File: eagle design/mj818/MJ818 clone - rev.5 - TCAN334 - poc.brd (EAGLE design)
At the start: 35 x 35 mm, 36 parts, among them IC202 LDK320AM33R, IC302 STM32F042G6U6, IC401 TCAN334, IC506 MAX16820, IC507 SQA470EEJ-T1_GE3, IC601 MAX16839, J101 Power Supply, J102 LED, J103 CAN

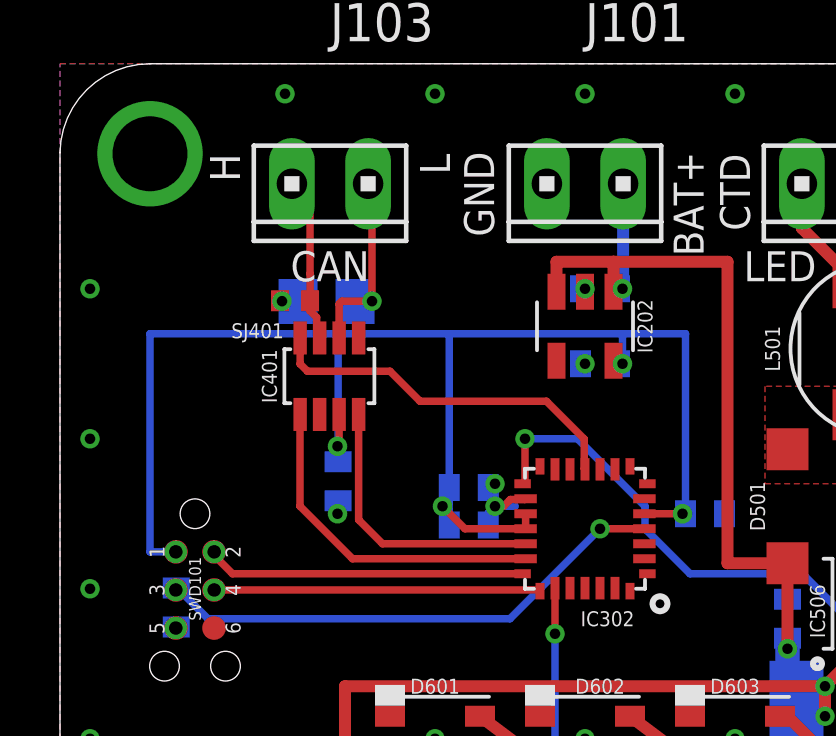
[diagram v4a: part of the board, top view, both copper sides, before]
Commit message: - added CAN split termination with two 60 Ohm resistors and one 47nF ceramic capacitor.
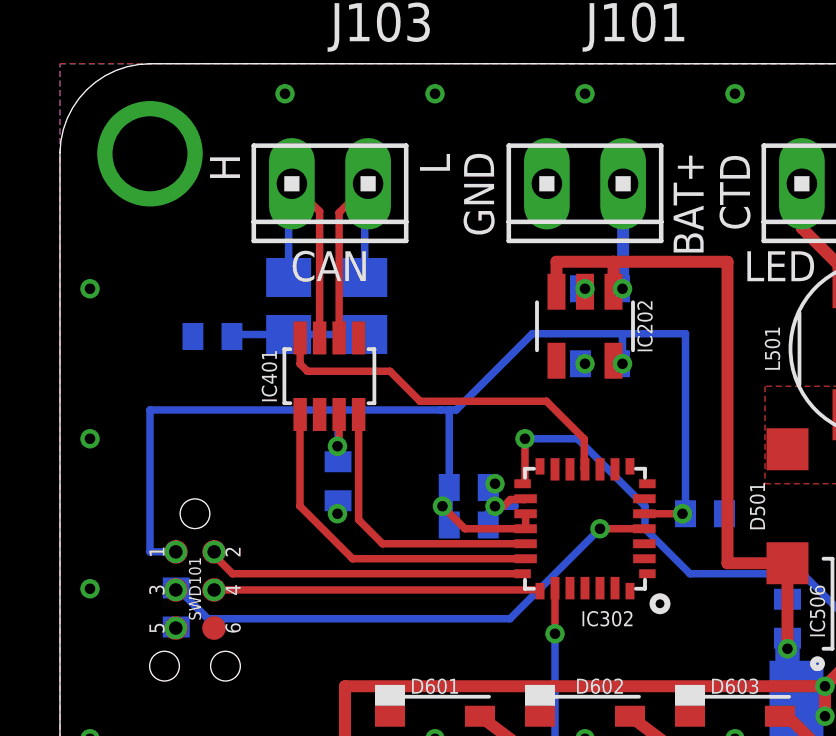
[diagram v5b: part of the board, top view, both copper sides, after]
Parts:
- removed SJ401: CAN termination, rcl:R0402
- added C401: 47nF, rcl:C0402
- added R401: 60, rcl:R0805
- R405: value 120 -> 60
- moved R405 1.28 mm to (10.2, 26.9), turned to 270 degrees
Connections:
- removed net CAN_INFRA:CAN_JMPR: R405.2, SJ401.1
- new net CAN_INFRA:SPLIT: C401.1, R401.1, R405.2
- net CAN_H: now also R401.2; no longer SJ401.2
- net GND: now also C401.2
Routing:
- net 3V3: track 51.1 -> 44.5 mm
- net CAN_INFRA:SPLIT: track 0.00 -> 4.46 mm
- net CAN_H: track 5.52 -> 8.69 mm
- net CAN_L: track 6.81 -> 8.71 mm, vias 1 -> 0
- net CAN_INFRA:CAN_JMPR: track 0.63 -> 0.00 mm, vias 1 -> 0
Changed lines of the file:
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@@
 <setting verticaltext="up"/>
 </settings>
-<grid distance="0.25" unitdist="mm" unit="mm" style="dots" multiple="1" display="yes" altdistance="0.125" altunitdist="mm" altunit="mm"/>
+<grid distance="20" unitdist="mil" unit="mil" style="dots" multiple="1" display="yes" altdistance="0.125" altunitdist="mm" altunit="mm"/>
 <layers>
 <layer number="1" name="Top" color="4" fill="1" visible="yes" active="yes"/>
@@
 <attribute name="VALUE" x="29.25" y="17" size="1.27" layer="28" rot="MR270"/>
 </element>
-<element name="R405" library="rcl" library_urn="urn:adsk.eagle:library:334" package="R0805" package3d_urn="urn:adsk.eagle:package:23553/2" value="120" x="8.885" y="27.075" locked="yes" smashed="yes" rot="MR0">
-<attribute name="NAME" x="8.885" y="28.575" locked="yes" size="0.5" layer="26" font="fixed" rot="MR0" align="center"/>
-<attribute name="POPULARITY" value="86" x="8.885" y="27.075" locked="yes" size="1.778" layer="28" rot="MR0" display="off"/>
-<attribute name="SPICEPREFIX" value="R" x="8.885" y="27.075" locked="yes" size="1.778" layer="28" rot="MR0" display="off"/>
-<attribute name="VALUE" x="8.885" y="27.075" locked="yes" size="1.27" layer="28" rot="MR0"/>
+<element name="R405" library="rcl" library_urn="urn:adsk.eagle:library:334" package="R0805" package3d_urn="urn:adsk.eagle:package:23553/2" value="60" x="10.16" y="26.924" smashed="yes" rot="MR270">
+<attribute name="NAME" x="10.16" y="24.892" size="0.5" layer="26" font="fixed" rot="MR180" align="center"/>
+<attribute name="POPULARITY" value="86" x="10.16" y="26.924" size="1.778" layer="28" rot="MR270" display="off"/>
+<attribute name="SPICEPREFIX" value="R" x="10.16" y="26.924" size="1.778" layer="28" rot="MR270" display="off"/>
+<attribute name="VALUE" x="10.16" y="26.924" size="1.27" layer="28" rot="MR270"/>
 </element>
 <element name="R508" library="rcl" library_urn="urn:adsk.eagle:library:334" package="R2010" package3d_urn="urn:adsk.eagle:package:23551/2" value="WSLT2010R2200FEB18 / 0.22Ohm 1W" x="26.75" y="13.75" smashed="yes" rot="MR0">
@@
 <attribute name="VALUE" x="27" y="9.5" size="1.27" layer="28" rot="MR90"/>
 </element>
-<element name="SJ401" library="rcl" library_urn="urn:adsk.eagle:library:334" package="R0402" package3d_urn="urn:adsk.eagle:package:23547/3" value="CAN termination" x="7.835" y="27.1" locked="yes" smashed="yes">
-<attribute name="NAME" x="6.585" y="26.1" locked="yes" size="0.5" layer="25" font="fixed" align="center"/>
-<attribute name="POPULARITY" value="0" x="7.835" y="27.1" locked="yes" size="1.778" layer="27" display="off"/>
-<attribute name="SPICEPREFIX" value="R" x="7.835" y="27.1" locked="yes" size="1.778" layer="27" display="off"/>
-<attribute name="VALUE" x="7.835" y="27.1" locked="yes" size="1.27" layer="27"/>
-</element>
 <element name="SWD101" library="tag-connect" package="TC2030-NL" value="TC2030-NL" x="4.5" y="20" locked="yes" smashed="yes" rot="R270">
 <attribute name="NAME" x="4.5" y="17.5" locked="yes" size="0.4" layer="25" font="fixed" rot="R90" align="center"/>
@@
 <attribute name="SPICEPREFIX" value="R" x="30.5" y="9.25" size="1.778" layer="28" rot="MR270" display="off"/>
 <attribute name="VALUE" x="32.405" y="9.885" size="1.27" layer="28" rot="MR270"/>
+</element>
+<element name="C401" library="rcl" library_urn="urn:adsk.eagle:library:334" package="C0402" package3d_urn="urn:adsk.eagle:package:23626/2" value="47nF" x="5.08" y="25.908" smashed="yes" rot="MR0">
+<attribute name="NAME" x="5.08" y="24.892" size="0.5" layer="26" rot="MR0" align="center"/>
+<attribute name="POPULARITY" value="18" x="5.08" y="25.908" size="1.778" layer="28" rot="MR0" display="off"/>
+<attribute name="SPICEPREFIX" value="C" x="5.08" y="25.908" size="1.778" layer="28" rot="MR0" display="off"/>
+<attribute name="VALUE" x="5.715" y="24.003" size="1.27" layer="28" rot="MR0"/>
+</element>
+<element name="R401" library="rcl" library_urn="urn:adsk.eagle:library:334" package="R0805" package3d_urn="urn:adsk.eagle:package:23553/2" value="60" x="7.62" y="26.924" smashed="yes" rot="MR90">
+<attribute name="NAME" x="7.62" y="24.892" size="0.5" layer="26" rot="MR0" align="center"/>
+<attribute name="POPULARITY" value="86" x="7.62" y="26.924" size="1.778" layer="28" rot="MR90" display="off"/>
+<attribute name="SPICEPREFIX" value="R" x="7.62" y="26.924" size="1.778" layer="28" rot="MR90" display="off"/>
+<attribute name="VALUE" x="5.08" y="26.289" size="1.27" layer="28" rot="MR90"/>
 </element>
 </elements>
@@
 <contactref element="J101" pad="1"/>
 <contactref element="R601" pad="1"/>
+<contactref element="C401" pad="2"/>
 </signal>
 <signal name="DIM_BRAKE" class="3">
@@
 <signal name="CAN_H" class="3">
 <contactref element="IC401" pad="P$7"/>
-<contactref element="SJ401" pad="2"/>
-<wire x1="8.655" y1="25.86" x2="8.555" y2="25.96" width="0.25" layer="1"/>
-<wire x1="8.555" y1="25.96" x2="8.555" y2="26.54461875" width="0.25" layer="1"/>
-<wire x1="8.335" y1="26.76461875" x2="8.335" y2="27.1" width="0.25" layer="1"/>
-<wire x1="8.555" y1="26.54461875" x2="8.335" y2="26.76461875" width="0.25" layer="1"/>
 <contactref element="J103" pad="1"/>
-<wire x1="7.73" y1="31" x2="8.335" y2="30.395" width="0.25" layer="1"/>
-<wire x1="8.335" y1="30.395" x2="8.335" y2="28" width="0.25" layer="1"/>
-<wire x1="8.335" y1="28" x2="8.335" y2="27.1" width="0.25" layer="1"/>
+<contactref element="R401" pad="2"/>
+<wire x1="7.62" y1="27.874" x2="7.62" y2="30.89" width="0.25" layer="16"/>
+<wire x1="7.62" y1="30.89" x2="7.73" y2="31" width="0.25" layer="16"/>
+<wire x1="8.655" y1="25.86" x2="8.655" y2="30.075" width="0.25" layer="1"/>
+<wire x1="8.655" y1="30.075" x2="7.73" y2="31" width="0.25" layer="1"/>
 </signal>
 <signal name="CAN_L" class="3">
 <contactref element="IC401" pad="P$6"/>
 <contactref element="R405" pad="1"/>
-<via x="10.4" y="27.085" extent="1-16" drill="0.35"/>
-<wire x1="9.305" y1="25.86" x2="9.305" y2="26.99" width="0.25" layer="1"/>
-<wire x1="9.305" y1="26.99" x2="9.4" y2="27.085" width="0.25" layer="1"/>
-<wire x1="9.4" y1="27.085" x2="10.4" y2="27.085" width="0.25" layer="1"/>
-<wire x1="9.835" y1="27.075" x2="9.835" y2="27.085" width="0.25" layer="16"/>
-<wire x1="9.835" y1="27.085" x2="10.4" y2="27.085" width="0.25" layer="16"/>
 <contactref element="J103" pad="2"/>
-<wire x1="10.27" y1="31" x2="10.4" y2="30.87" width="0.25" layer="1"/>
-<wire x1="10.4" y1="30.87" x2="10.4" y2="27.085" width="0.25" layer="1"/>
+<wire x1="10.16" y1="27.874" x2="10.16" y2="30.89" width="0.25" layer="16"/>
+<wire x1="10.16" y1="30.89" x2="10.27" y2="31" width="0.25" layer="16"/>
+<wire x1="9.305" y1="25.86" x2="9.305" y2="30.035" width="0.25" layer="1"/>
+<wire x1="9.305" y1="30.035" x2="10.27" y2="31" width="0.25" layer="1"/>
 </signal>
 <signal name="3V3" class="4">
@@
 <wire x1="9.305" y1="22.305" x2="9.25" y2="22.25" width="0.25" layer="1"/>
 <wire x1="9.27" y1="21.775" x2="9.25" y2="21.755" width="0.25" layer="16"/>
-<wire x1="12.975" y1="26" x2="18.75" y2="26" width="0.25" layer="16"/>
+<wire x1="15.748" y1="26" x2="18.75" y2="26" width="0.25" layer="16"/>
 <wire x1="18.75" y1="26" x2="20.85" y2="26" width="0.25" layer="16"/>
 <wire x1="12.975" y1="20.25" x2="12.975" y2="20.875" width="0.25" layer="16"/>
@@
 <wire x1="3.865" y1="18.73" x2="3.86" y2="18.73" width="0.25" layer="1"/>
 <wire x1="20.85" y1="20" x2="20.85" y2="26" width="0.25" layer="16"/>
-<wire x1="12.975" y1="26" x2="9.27" y2="26" width="0.25" layer="16"/>
-<wire x1="3" y1="26" x2="9.27" y2="26" width="0.25" layer="16"/>
-<wire x1="9.27" y1="26" x2="9.27" y2="21.775" width="0.25" layer="16"/>
-<wire x1="12.975" y1="20.875" x2="12.975" y2="26" width="0.25" layer="16"/>
+<wire x1="12.975" y1="23.46" x2="12.7" y2="23.46" width="0.25" layer="16"/>
+<wire x1="13.208" y1="23.46" x2="12.975" y2="23.46" width="0.25" layer="16"/>
+<wire x1="12.7" y1="23.46" x2="9.27" y2="23.46" width="0.25" layer="16"/>
+<wire x1="3" y1="23.46" x2="9.27" y2="23.46" width="0.25" layer="16"/>
+<wire x1="9.27" y1="23.46" x2="9.27" y2="21.775" width="0.25" layer="16"/>
+<wire x1="12.975" y1="20.875" x2="12.975" y2="23.46" width="0.25" layer="16"/>
 <wire x1="3.86" y1="18.73" x2="3" y2="18.73" width="0.25" layer="16"/>
-<wire x1="3" y1="18.73" x2="3" y2="26" width="0.25" layer="16"/>
+<wire x1="3" y1="18.73" x2="3" y2="23.46" width="0.25" layer="16"/>
 <wire x1="18.45" y1="25.1" x2="18.65" y2="25.1" width="0.25" layer="1"/>
 <wire x1="18.65" y1="25.1" x2="18.75" y2="25" width="0.25" layer="1"/>
@@
 <wire x1="9.25" y1="22.25" x2="9.25" y2="21.755" width="0.25" layer="16"/>
 <wire x1="9.25" y1="21.755" x2="9.27" y2="21.735" width="0.25" layer="16"/>
+<wire x1="13.208" y1="23.46" x2="15.748" y2="26" width="0.25" layer="16"/>
 </signal>
 <signal name="SYS_SWDIO" class="3">
@@
 <wire x1="12" y1="23.75" x2="16.21461875" y2="23.75" width="0.25" layer="1"/>
 </signal>
-<signal name="CAN_INFRA:CAN_JMPR" class="3">
+<signal name="CAN_INFRA:SPLIT" class="3">
 <contactref element="R405" pad="2"/>
-<contactref element="SJ401" pad="1"/>
-<via x="7.4" y="27.085" extent="1-16" drill="0.35"/>
-<wire x1="7.335" y1="27.1" x2="7.36" y2="27.125" width="0.25" layer="1"/>
-<wire x1="7.36" y1="27.125" x2="7.4" y2="27.085" width="0.25" layer="1"/>
-<wire x1="7.4" y1="27.085" x2="7.925" y2="27.085" width="0.25" layer="16"/>
-<wire x1="7.925" y1="27.085" x2="7.935" y2="27.075" width="0.25" layer="16"/>
+<contactref element="C401" pad="1"/>
+<contactref element="R401" pad="1"/>
+<wire x1="5.73" y1="25.908" x2="5.796" y2="25.974" width="0.25" layer="16"/>
+<wire x1="5.796" y1="25.974" x2="7.62" y2="25.974" width="0.25" layer="16"/>
+<wire x1="7.62" y1="25.974" x2="10.16" y2="25.974" width="0.25" layer="16"/>
 </signal>
 <signal name="BRAKE_LED_DRIVER:DIM_BRAKE_DRAIN" class="3">

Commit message: - unified values of passive elements to a common format
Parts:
- C202, C506: value 1μF / 10V -> 1uF / 10V
- C207, C601: value 1μF -> 1uF / 10V
- C301, C305, C307: value 0.1u -> 0.1uF / 10V
- C304: value 1u -> 1uF / 10V
- C401: value 47nF -> 47nF / 10V
- C405: value 0.1μF -> 0.1uF / 10V
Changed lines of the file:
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@@
 </autorouter>
 <elements>
-<element name="C202" library="rcl" library_urn="urn:adsk.eagle:library:334" package="C0402" package3d_urn="urn:adsk.eagle:package:23626/2" value="1μF / 10V" x="18" y="27.5" locked="yes" smashed="yes" rot="MR0">
+<element name="C202" library="rcl" library_urn="urn:adsk.eagle:library:334" package="C0402" package3d_urn="urn:adsk.eagle:package:23626/2" value="1uF / 10V" x="18" y="27.5" locked="yes" smashed="yes" rot="MR0">
 <attribute name="NAME" x="18" y="28.5" locked="yes" size="0.5" layer="26" font="fixed" rot="MR0" align="center"/>
 <attribute name="POPULARITY" value="18" x="18" y="27.5" locked="yes" size="1.778" layer="28" rot="MR0" display="off"/>
@@
 <attribute name="VALUE" x="18" y="27.5" locked="yes" size="1.27" layer="28" rot="MR0"/>
 </element>
-<element name="C207" library="rcl" library_urn="urn:adsk.eagle:library:334" package="C0402" package3d_urn="urn:adsk.eagle:package:23626/2" value="1μF" x="18" y="25" locked="yes" smashed="yes" rot="MR180">
+<element name="C207" library="rcl" library_urn="urn:adsk.eagle:library:334" package="C0402" package3d_urn="urn:adsk.eagle:package:23626/2" value="1uF / 10V" x="18" y="25" locked="yes" smashed="yes" rot="MR180">
 <attribute name="NAME" x="18" y="24" locked="yes" size="0.5" layer="26" font="fixed" rot="MR180" align="center"/>
 <attribute name="POPULARITY" value="18" x="18" y="25" locked="yes" size="1.778" layer="28" rot="MR180" display="off"/>
@@
 <attribute name="VALUE" x="18" y="25" locked="yes" size="1.27" layer="28" rot="MR180"/>
 </element>
-<element name="C301" library="rcl" library_urn="urn:adsk.eagle:library:334" package="C0402" package3d_urn="urn:adsk.eagle:package:23626/2" value="0.1u" x="13.625" y="20.875" locked="yes" smashed="yes" rot="MR0">
+<element name="C301" library="rcl" library_urn="urn:adsk.eagle:library:334" package="C0402" package3d_urn="urn:adsk.eagle:package:23626/2" value="0.1uF / 10V" x="13.625" y="20.875" locked="yes" smashed="yes" rot="MR0">
 <attribute name="NAME" x="13.625" y="21.875" locked="yes" size="0.5" layer="26" font="fixed" rot="MR0" align="center"/>
 <attribute name="POPULARITY" value="18" x="13.625" y="20.875" locked="yes" size="1.778" layer="28" rot="MR0" display="off"/>
@@
 <attribute name="VALUE" x="13.625" y="20.875" locked="yes" size="1.27" layer="28" rot="MR0"/>
 </element>
-<element name="C304" library="rcl" library_urn="urn:adsk.eagle:library:334" package="C0402" package3d_urn="urn:adsk.eagle:package:23626/2" value="1u" x="21.5" y="20" locked="yes" smashed="yes" rot="MR0">
+<element name="C304" library="rcl" library_urn="urn:adsk.eagle:library:334" package="C0402" package3d_urn="urn:adsk.eagle:package:23626/2" value="1uF / 10V" x="21.5" y="20" locked="yes" smashed="yes" rot="MR0">
 <attribute name="NAME" x="21.5" y="21" locked="yes" size="0.5" layer="26" font="fixed" rot="MR0" align="center"/>
 <attribute name="POPULARITY" value="18" x="21.5" y="20" locked="yes" size="1.778" layer="28" rot="MR0" display="off"/>
@@
 <attribute name="VALUE" x="21.5" y="20" locked="yes" size="1.27" layer="28" rot="MR0"/>
 </element>
-<element name="C305" library="rcl" library_urn="urn:adsk.eagle:library:334" package="C0402" package3d_urn="urn:adsk.eagle:package:23626/2" value="0.1u" x="13.625" y="19.625" locked="yes" smashed="yes" rot="MR0">
+<element name="C305" library="rcl" library_urn="urn:adsk.eagle:library:334" package="C0402" package3d_urn="urn:adsk.eagle:package:23626/2" value="0.1uF / 10V" x="13.625" y="19.625" locked="yes" smashed="yes" rot="MR0">
 <attribute name="NAME" x="13.625" y="18.625" locked="yes" size="0.5" layer="26" font="fixed" rot="MR0" align="center"/>
 <attribute name="POPULARITY" value="18" x="13.625" y="19.625" locked="yes" size="1.778" layer="28" rot="MR0" display="off"/>
@@
 <attribute name="VALUE" x="13.625" y="19.625" locked="yes" size="1.27" layer="28" rot="MR0"/>
 </element>
-<element name="C307" library="rcl" library_urn="urn:adsk.eagle:library:334" package="C0402" package3d_urn="urn:adsk.eagle:package:23626/2" value="0.1u" x="3.875" y="16.875" locked="yes" smashed="yes" rot="MR90">
+<element name="C307" library="rcl" library_urn="urn:adsk.eagle:library:334" package="C0402" package3d_urn="urn:adsk.eagle:package:23626/2" value="0.1uF / 10V" x="3.875" y="16.875" locked="yes" smashed="yes" rot="MR90">
 <attribute name="NAME" x="2.875" y="16.875" locked="yes" size="0.5" layer="26" font="fixed" rot="MR90" align="center"/>
 <attribute name="POPULARITY" value="18" x="3.875" y="16.875" locked="yes" size="1.778" layer="28" rot="MR90" display="off"/>
@@
 <attribute name="VALUE" x="3.875" y="16.875" locked="yes" size="1.27" layer="28" rot="MR90"/>
 </element>
-<element name="C405" library="rcl" library_urn="urn:adsk.eagle:library:334" package="C0402" package3d_urn="urn:adsk.eagle:package:23626/2" value="0.1μF" x="9.27" y="21.085" locked="yes" smashed="yes" rot="MR270">
+<element name="C405" library="rcl" library_urn="urn:adsk.eagle:library:334" package="C0402" package3d_urn="urn:adsk.eagle:package:23626/2" value="0.1uF / 10V" x="9.27" y="21.085" locked="yes" smashed="yes" rot="MR270">
 <attribute name="NAME" x="8.27" y="21.085" locked="yes" size="0.5" layer="26" font="fixed" rot="MR270" align="center"/>
 <attribute name="POPULARITY" value="18" x="9.27" y="21.085" locked="yes" size="1.778" layer="28" rot="MR270" display="off"/>
@@
 <attribute name="VALUE" x="9.27" y="21.085" locked="yes" size="1.27" layer="28" rot="MR270"/>
 </element>
-<element name="C506" library="rcl" library_urn="urn:adsk.eagle:library:334" package="C0402" package3d_urn="urn:adsk.eagle:package:23626/2" value="1μF / 10V" x="24.25" y="16.5" smashed="yes" rot="MR90">
+<element name="C506" library="rcl" library_urn="urn:adsk.eagle:library:334" package="C0402" package3d_urn="urn:adsk.eagle:package:23626/2" value="1uF / 10V" x="24.25" y="16.5" smashed="yes" rot="MR90">
 <attribute name="NAME" x="23.25" y="16.5" size="0.5" layer="26" font="fixed" rot="MR90" align="center"/>
 <attribute name="POPULARITY" value="18" x="24.25" y="16.5" size="1.778" layer="28" rot="MR90" display="off"/>
@@
 <attribute name="VALUE" x="24.25" y="16.5" size="1.27" layer="28" rot="MR90"/>
 </element>
-<element name="C601" library="rcl" library_urn="urn:adsk.eagle:library:334" package="C0402" package3d_urn="urn:adsk.eagle:package:23626/2" value="1μF" x="28.75" y="6.5" smashed="yes" rot="MR180">
+<element name="C601" library="rcl" library_urn="urn:adsk.eagle:library:334" package="C0402" package3d_urn="urn:adsk.eagle:package:23626/2" value="1uF / 10V" x="28.75" y="6.5" smashed="yes" rot="MR180">
 <attribute name="NAME" x="28.75" y="7.5" size="0.5" layer="26" font="fixed" rot="MR180" align="center"/>
 <attribute name="POPULARITY" value="18" x="28.75" y="6.5" size="1.778" layer="28" rot="MR180" display="off"/>
@@
 <attribute name="VALUE" x="32.405" y="9.885" size="1.27" layer="28" rot="MR270"/>
 </element>
-<element name="C401" library="rcl" library_urn="urn:adsk.eagle:library:334" package="C0402" package3d_urn="urn:adsk.eagle:package:23626/2" value="47nF" x="5.08" y="25.908" smashed="yes" rot="MR0">
+<element name="C401" library="rcl" library_urn="urn:adsk.eagle:library:334" package="C0402" package3d_urn="urn:adsk.eagle:package:23626/2" value="47nF / 10V" x="5.08" y="25.908" smashed="yes" rot="MR0">
 <attribute name="NAME" x="5.08" y="24.892" size="0.5" layer="26" rot="MR0" align="center"/>
 <attribute name="POPULARITY" value="18" x="5.08" y="25.908" size="1.778" layer="28" rot="MR0" display="off"/>
